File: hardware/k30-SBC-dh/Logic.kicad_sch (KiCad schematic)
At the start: 20 parts, among them SW2 SW_DIP_x06, U10 74HC253, U11 74HC138, U12 74HC393, U17 74LVC1G32, U2 74HC14, U3 74HC05, U4 74HC139, U5 4072, U6 74HC20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

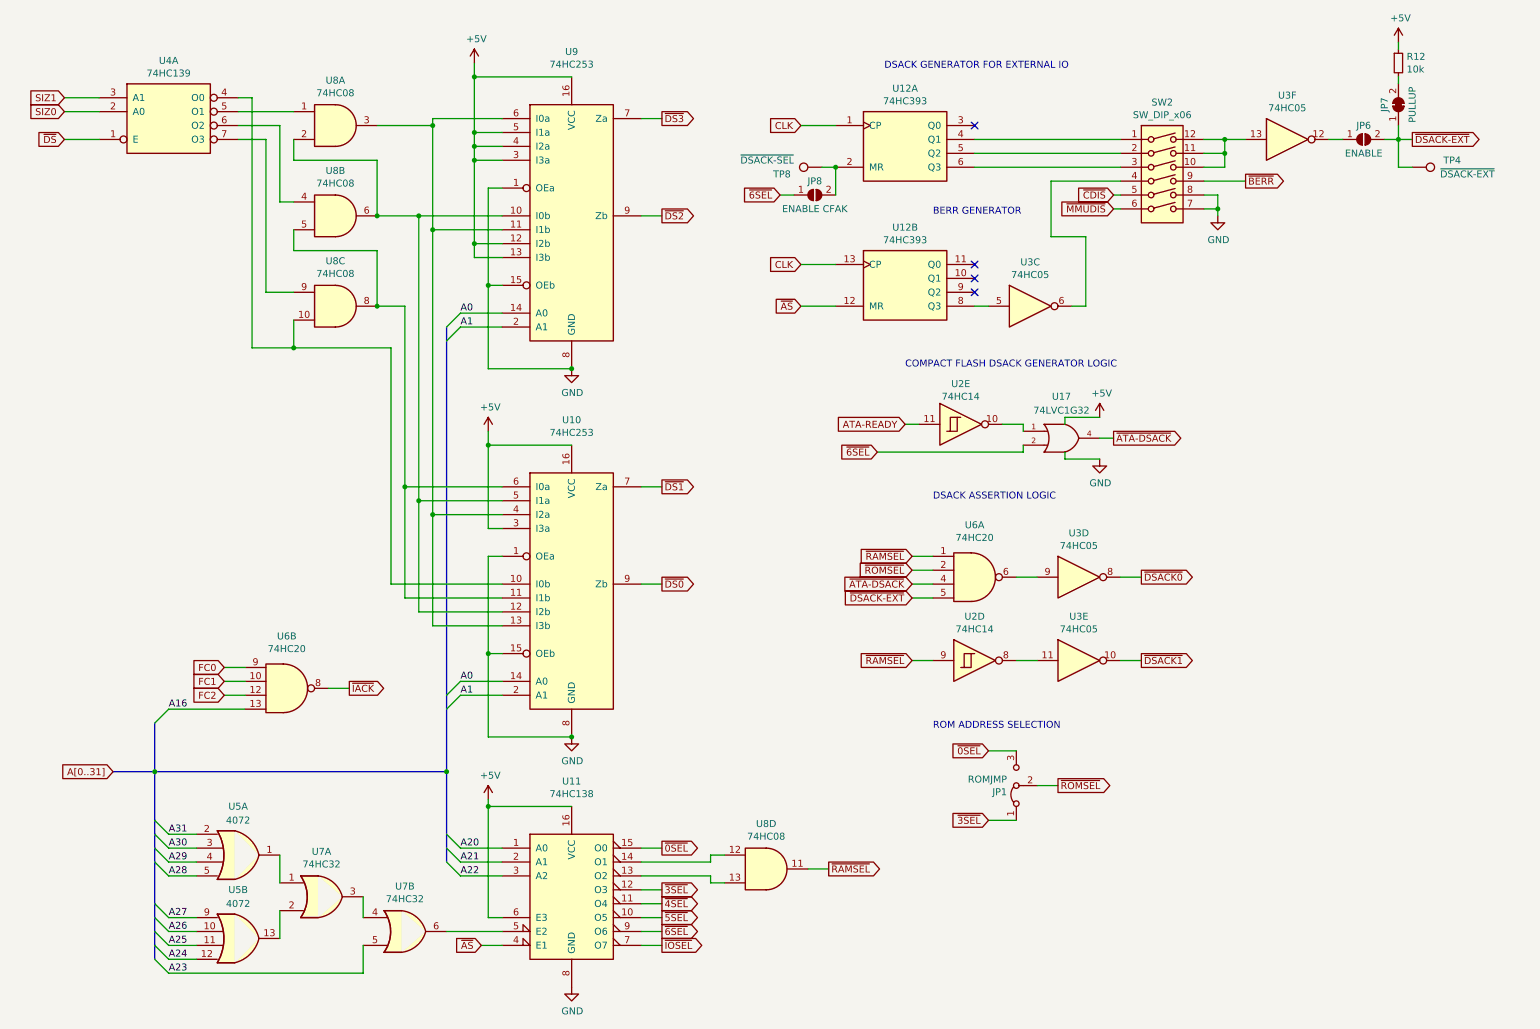
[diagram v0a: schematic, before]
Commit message: use 5.08mm 1x2 screw terminal for power
These are good for 6A.

Noted on the silkscreen that this is a modified version
of the PCB.
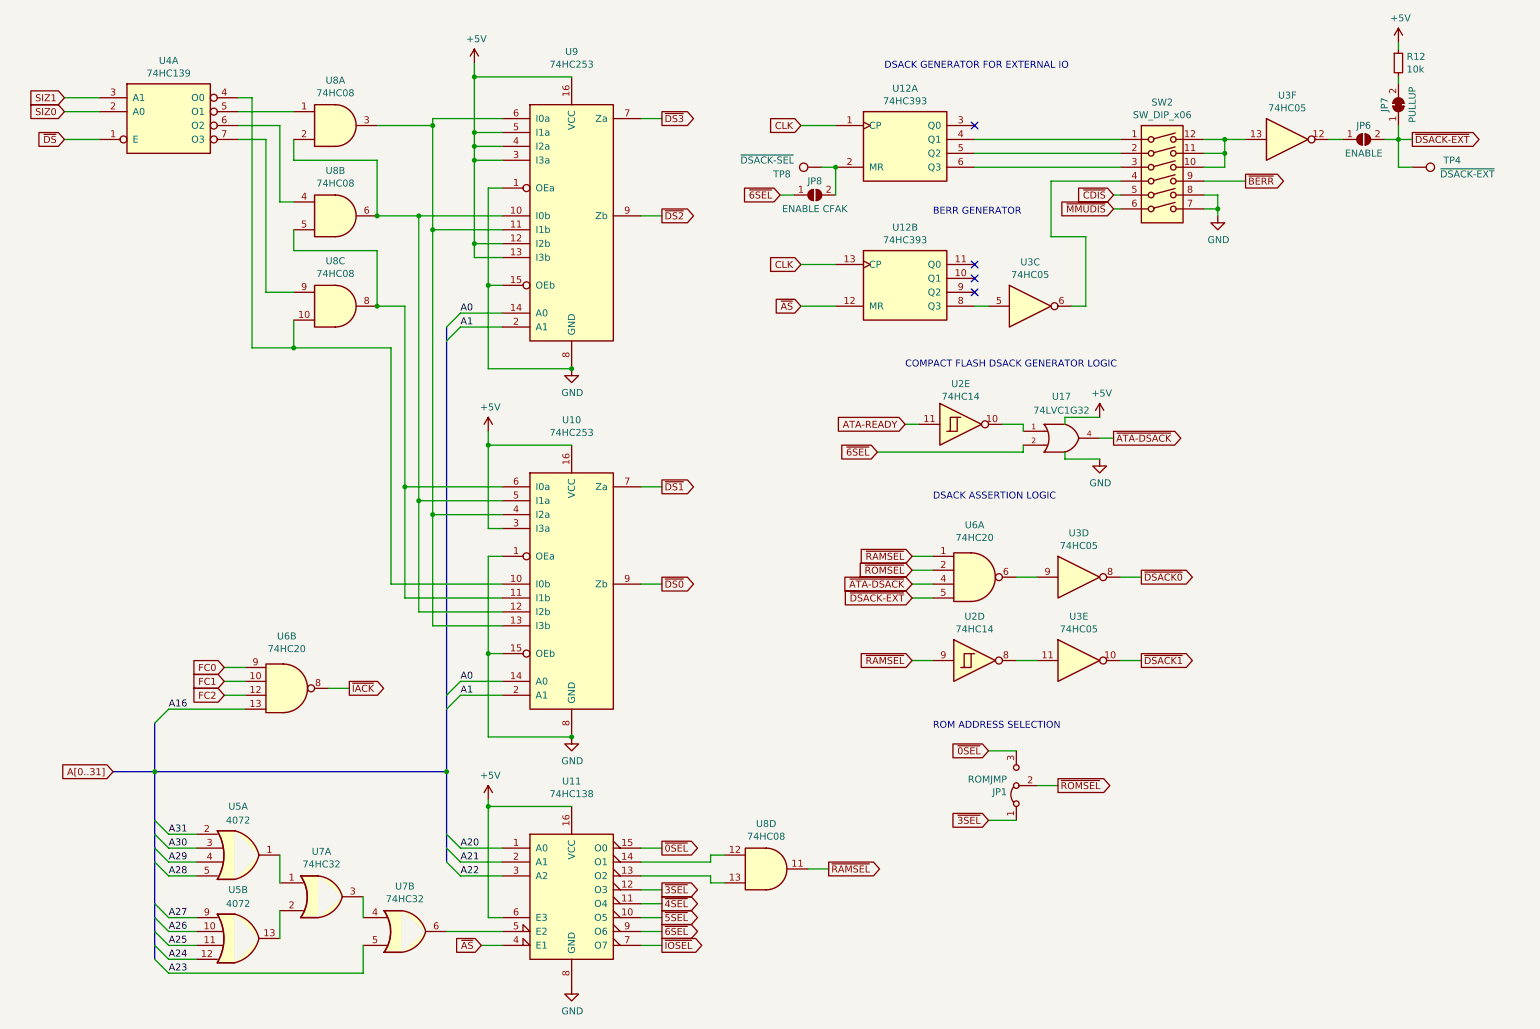
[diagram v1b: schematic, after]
